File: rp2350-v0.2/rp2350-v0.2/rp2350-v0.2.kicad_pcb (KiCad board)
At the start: 4 copper layers, 65 x 65 mm, 112 parts, among them IC1 M95512-RMN6TP, IC2 TFBS4711-TT1, IC3 BQ25628ERYKR, IC4 RT6150B-33GQW, IC5 W25Q128JVSIM_TR, J1 USB_C_Receptacle_USB2.0_16P, J2 SWD, J3 BAT, J4 DO0180FMST08, J5 DBG_UART, J6 SPEAKER_CONNECTOR, SW1 BUT_R, SW2 BUT_M, SW3 BUT_L, SW4 SW_Push, U1 RP2350A-QFN60, Y1 ABM8-272-T3, Y2 SIT1533AI-H4-DCC-32.768E

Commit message: v0.2: loads of progress now gonna change it all up again
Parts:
- R34: value R -> 1k
- TP3: value GP28 -> GP26
- moved R23 15.4 mm to (166.2, 65.3), turned to 90 degrees
- moved JP1 12.2 mm to (179.8, 106.2)
- moved R20 9.06 mm to (159.2, 74.6), turned to 90 degrees
- moved R3 7.91 mm to (172.6, 95.0), turned to 0 degrees
- moved R5 7.69 mm to (143.8, 54.1), turned to 90 degrees
- moved C1 7.27 mm to (167.5, 104.6)
- moved C3 7.08 mm to (138.9, 53.8), turned to 180 degrees
- moved C2 6.95 mm to (145.4, 53.6)
- moved R4 6.76 mm to (162.9, 93.5), turned to 180 degrees
- moved JP3 6.73 mm to (170.7, 85.6), turned to 180 degrees
- moved C19 6.07 mm to (169.4, 73.9), turned to 90 degrees
- moved R13 5.83 mm to (97.6, 99.7)
- moved TH1 5.79 mm to (99.7, 104.0)
- moved TP1 5.76 mm to (128.7, 99.2)
- moved C5 5.69 mm to (164.9, 92.0), turned to 180 degrees
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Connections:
- R34 pad 1: Net-(U1-GPIO29_ADC3) -> /mcu/GPIO25
- TP3 pad 1: /mcu/GPIO28 -> /mcu/GPIO26
- U1 pad 12: /irda/IRDA.SD -> /mcu/QSPI1.SCK
- U1 pad 13: /irda/IRDA.RX -> /mcu/QSPI1.SDIO3
- U1 pad 14: /irda/IRDA.TX -> /mcu/QSPI1.SDIO2
- U1 pad 15: /buttons/BUT.L -> /mcu/QSPI1.SDIO1
- U1 pad 17: /mcu/QSPI1.SDIO1 -> /irda/IRDA.SD
- U1 pad 18: /mcu/QSPI1.SDIO2 -> /irda/IRDA.RX
- U1 pad 19: /mcu/QSPI1.SDIO3 -> /irda/IRDA.TX
- U1 pad 27: /mcu/QSPI1.SCK -> /buttons/BUT.L
- U1 pad 36: /mcu/PWR_AUX.~{BAT_CE} -> /mcu/SOUND_PWM
- U1 pad 37: /mcu/PWR_AUX.~{BAT_INT} -> /mcu/GPIO25
- U1 pad 40: /buttons/BUT.R -> /mcu/GPIO26
- U1 pad 41: /mcu/SOUND_PWM -> /buttons/BUT.R
- U1 pad 42: /mcu/GPIO28 -> /mcu/PWR_AUX.~{BAT_INT}
- U1 pad 43: Net-(U1-GPIO29_ADC3) -> /mcu/PWR_AUX.~{BAT_CE}
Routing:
- net /mcu/PWR_AUX.~{BAT_INT}: track 1.66 -> 50.4 mm, vias 1 -> 2
- net /accel/SPI.SCK: track 6.66 -> 48.3 mm
- net /mcu/I2C.SCL: track 3.07 -> 44.6 mm, vias 1 -> 2
- net /mcu/PWR_AUX.~{BAT_CE}: track 4.82 -> 44.4 mm, vias 1 -> 2
- net /mcu/I2C.SDA: track 3.27 -> 42.8 mm, vias 1 -> 2
- net /eeprom/~{EEPROM_CSB}: track 4.76 -> 43.7 mm, vias 0 -> 2
- net /connectors/DBG_UART.RX: track 0.00 -> 37.8 mm
- net /connectors/DBG_UART.TX: track 0.00 -> 37.0 mm
- net /accel/~{ACCEL_CSB}: track 0.00 -> 35.8 mm, vias 0 -> 2
- net /accel/SPI.MISO: track 5.83 -> 41.1 mm
- net /accel/ACCEL_INT: track 0.00 -> 33.7 mm, vias 0 -> 2
- net /mcu/SCREEN_AUX.~{RST}: track 1.51 -> 29.9 mm, vias 0 -> 2
- net /accel/SPI.MOSI: track 7.92 -> 36.2 mm, vias 0 -> 2
- net /mcu/SCREEN_AUX.~{CSB}: track 2.02 -> 28.0 mm, vias 0 -> 2
- net /mcu/QSPI1.SCK: track 1.53 -> 26.0 mm
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- added copper zone on In2.Cu, net /accel/ACCEL_3V3
- added copper zone on In2.Cu, net /irda/IRDA_3V3
- added copper zone on F.Cu, net /screen/SCREEN_VSYS

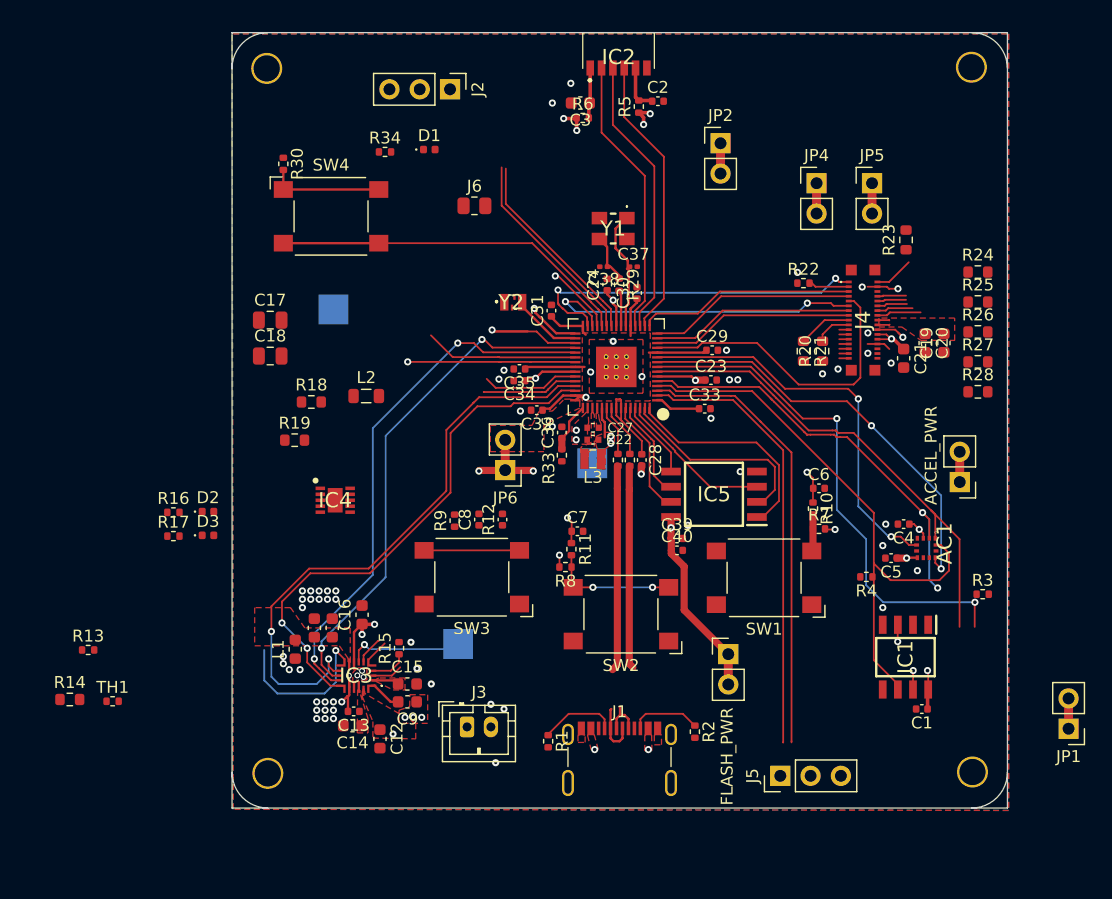
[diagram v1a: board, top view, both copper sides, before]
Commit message: v0.2: more progress on routing, nearly done
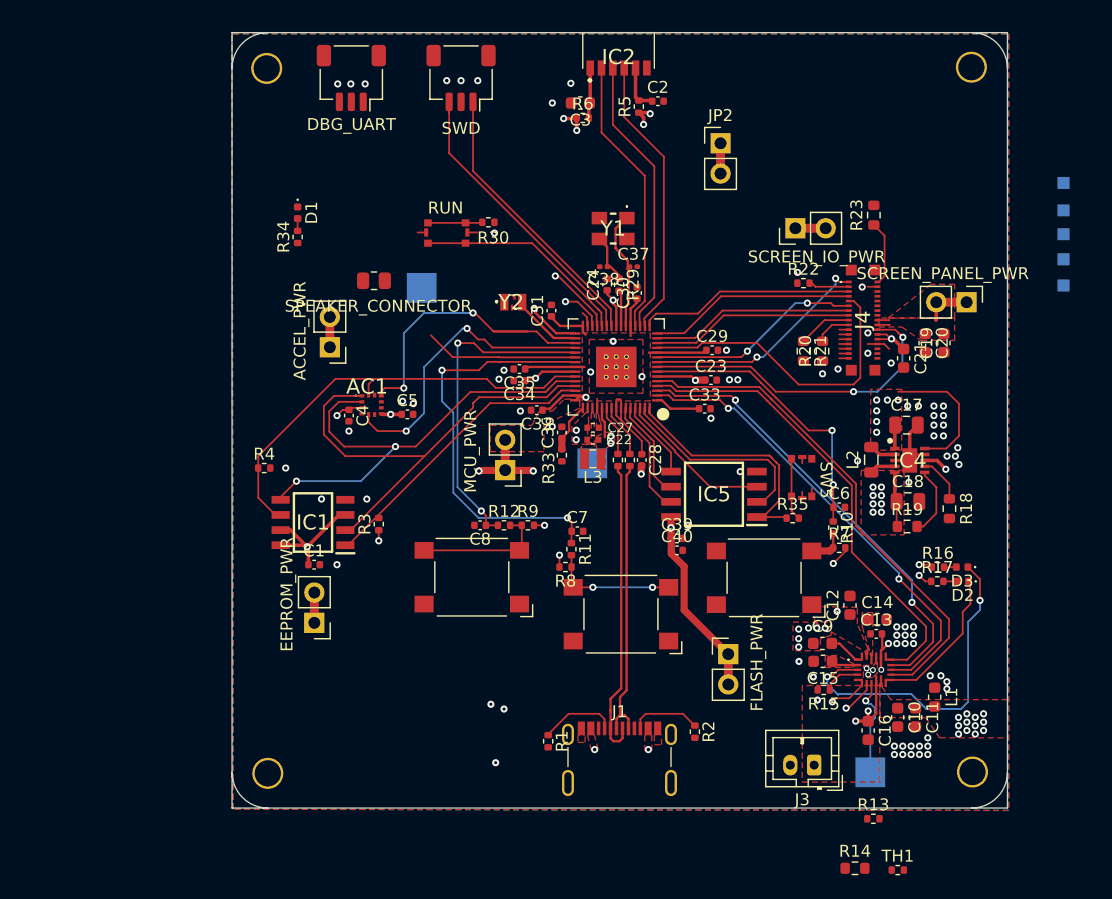
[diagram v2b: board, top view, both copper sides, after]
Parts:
- removed R24, R25, R26, R27, R28: 0R, Resistor_SMD:R_0603_1608Metric
- added R35: 1k, Resistor_SMD:R_0402_1005Metric, F.Cu at (156.7, 88.6)
- added SW5: BOOTSEL, CustomFootprints:WS_TASV_435151014824, F.Cu at (158.3, 85.2)
- added TP4: TP_SDA, TestPoint:TestPoint_Pad_1.0x1.0mm, B.Cu at (179.4, 62.8)
- added TP5: TP_SCL, TestPoint:TestPoint_Pad_1.0x1.0mm, B.Cu at (179.4, 60.5)
- added TP6: TP_INT, TestPoint:TestPoint_Pad_1.0x1.0mm, B.Cu at (179.4, 64.8)
- added TP7: TP_RESET, TestPoint:TestPoint_Pad_1.0x1.0mm, B.Cu at (179.4, 66.9)
- added TP8: TP_VCC, TestPoint:TestPoint_Pad_1.0x1.0mm, B.Cu at (179.4, 69.1)
- J2, J5: footprint Connector_PinHeader_2.54mm:PinHeader_1x03_P2.54mm_Vertical -> Connector_JST:JST_SH_SM03B-SRSS-TB_1x03-1MP_P1.00mm_Horizontal
- R12: footprint Capacitor_SMD:C_0402_1005Metric -> Resistor_SMD:R_0402_1005Metric
- R31, R32: value R -> 22R
- SW4: value SW_Push -> RUN; footprint Button_Switch_SMD:SW_SPST_Omron_B3FS-101xP -> CustomFootprints:WS_TASV_435151014824
- moved J5 68.7 mm to (119.7, 51.7), turned to 180 degrees
- moved R13 67.3 mm to (163.5, 113.8)
- moved R14 67.3 mm to (161.9, 118.0)
- moved TH1 67.3 mm to (165.5, 118.1)
- moved R16 64.2 mm to (168.9, 92.7)
- moved R17 64.1 mm to (168.8, 93.9)
- moved JP1 63.8 mm to (116.6, 97.4)
- moved D2 63.5 mm to (171.0, 93.9), turned to 180 degrees
- moved D3 63.3 mm to (170.9, 92.7), turned to 180 degrees
- moved C18 54.8 mm to (166.4, 87.2)
- moved R18 54.2 mm to (169.8, 87.8), turned to -90 degrees
- moved C17 54.1 mm to (166.2, 80.8)
- moved JP3 54.0 mm to (117.9, 74.3)
- moved L1 53.7 mm to (168.6, 103.6), turned to -90 degrees
- moved C1 52.4 mm to (116.6, 92.5), turned to 0 degrees
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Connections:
- net /connectors/USB.DM renamed /connectors/USB.D-
- net /connectors/USB.DP renamed /connectors/USB.D+
- J4 pad 10: Net-(J4-TP_SDA) -> /screen/TP_I2C.SDA
- J4 pad 12: Net-(J4-TP_INT) -> /screen/TP_AUX.INT
- J4 pad 14: Net-(J4-TP_RESET) -> /screen/TP_AUX.RESET
- J4 pad 16: Net-(J4-TP_VCC) -> /screen/SCREEN_3V3
- J4 pad 8: Net-(J4-TP_SCL) -> /screen/TP_I2C.SCL
- J5 pad 1: /connectors/DBG_UART.TX -> /connectors/DBG_UART.RX
- J5 pad 3: /connectors/DBG_UART.RX -> /connectors/DBG_UART.TX
- SW4 pad 2: Net-(U1-RUN) -> Net-(R30-Pad2)
- U1 pad 10: /accel/ACCEL_INT -> /mcu/SCREEN_AUX.~{CSB}
- U1 pad 2: /connectors/DBG_UART.TX -> /mcu/I2C.SDA
- U1 pad 27: /buttons/BUT.L -> /connectors/DBG_UART.TX
- U1 pad 28: /mcu/SCREEN_AUX.~{CSB} -> /connectors/DBG_UART.RX
- U1 pad 29: /mcu/SCREEN_AUX.~{RST} -> unconnected-(U1-GPIO18-Pad29)
- U1 pad 3: /connectors/DBG_UART.RX -> /mcu/I2C.SCL
- U1 pad 31: /mcu/SCREEN_AUX.PWR_EN -> unconnected-(U1-GPIO19-Pad31)
- U1 pad 33: /buttons/BUT.M -> /accel/~{ACCEL_CSB}
- U1 pad 34: /mcu/I2C.SDA -> /accel/ACCEL_INT
- U1 pad 35: /mcu/I2C.SCL -> /buttons/BUT.L
- U1 pad 37: /mcu/GPIO25 -> /buttons/BUT.M
- U1 pad 4: /accel/SPI.SCK -> /mcu/PWR_AUX.~{BAT_CE}
- U1 pad 40: /mcu/GPIO26 -> /accel/SPI.SCK
- U1 pad 41: /buttons/BUT.R -> /accel/SPI.MOSI
- U1 pad 42: /mcu/PWR_AUX.~{BAT_INT} -> /accel/SPI.MISO
- U1 pad 43: /mcu/PWR_AUX.~{BAT_CE} -> /eeprom/~{EEPROM_CSB}
- U1 pad 5: /accel/SPI.MOSI -> /mcu/PWR_AUX.~{BAT_INT}
- U1 pad 7: /accel/SPI.MISO -> /buttons/BUT.R
- U1 pad 8: /eeprom/~{EEPROM_CSB} -> /mcu/SCREEN_AUX.PWR_EN
- U1 pad 9: /accel/~{ACCEL_CSB} -> /mcu/SCREEN_AUX.~{RST}
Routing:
- net /connectors/DBG_UART.RX: track 37.8 -> 3.51 mm, vias 0 -> 1
- net /connectors/DBG_UART.TX: track 37.0 -> 5.74 mm, vias 0 -> 1
- net /power/~{PG}: track 2.60 -> 28.3 mm, vias 0 -> 2
- net /buttons/BUT.M: track 12.5 -> 35.0 mm
- net /buttons/BUT.L: track 5.74 -> 27.4 mm, vias 1 -> 2
- net /mcu/SCREEN_AUX.PWR_EN: track 7.38 -> 27.8 mm
- net /eeprom/~{EEPROM_CSB}: track 43.7 -> 24.6 mm, vias 2 -> 0
- net +3.3V: track 6.46 -> 24.1 mm, vias 4 -> 13
- net /mcu/GPIO25: track 14.2 -> 0.00 mm, vias 1 -> 0
- net /buttons/BUT.R: track 10.8 -> 24.5 mm, vias 1 -> 2
- net Net-(U1-RUN): track 30.2 -> 18.1 mm
- net /accel/SPI.SCK: track 48.3 -> 37.6 mm
- net /mcu/SCREEN_AUX.~{RST}: track 29.9 -> 19.4 mm
- net /mcu/SCREEN_AUX.~{CSB}: track 28.0 -> 18.1 mm
- net /accel/~{ACCEL_CSB}: track 35.8 -> 25.9 mm
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- added copper zone on F.Cu, net +3.3V
- added copper zone on F.Cu, net /connectors/BAT+
- added copper zone on In2.Cu, net /screen/SCREEN_3V3
- added copper zone on In2.Cu, net VSYS
- removed copper zone on In2.Cu, net /connectors/BAT+
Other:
- board text removed: "500 mAh battery"

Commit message: v0.2: routing done, nearly ready for prod
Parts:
- added TP9: GP18, TestPoint:TestPoint_Pad_2.5x2.5mm, B.Cu at (119.8, 66.5)
- D1: value LED -> USER_LED
- JP4: value SCREEN_IO_PWR -> IO_PWR
- JP5: value SCREEN_PANEL_PWR -> PANEL_PWR
- TP3: value GP26 -> GP19
- moved TH1 44.9 mm to (122.8, 104.1), turned to 180 degrees
- moved R13 40.6 mm to (124.5, 102.4), turned to -90 degrees
- moved R14 39.2 mm to (124.5, 106.4), turned to -90 degrees
- moved J6 8.34 mm to (113.3, 67.9), turned to 90 degrees
- moved TP4 7.63 mm to (172.3, 60.0)
- moved TP8 7.63 mm to (172.3, 66.3)
- moved TP7 7.60 mm to (172.3, 64.2)
- moved TP6 7.60 mm to (172.3, 62.1)
- moved TP5 7.56 mm to (172.3, 57.9)
- moved C2 0.60 mm to (145.4, 54.2)
- moved C3 0.60 mm to (138.9, 54.4)
- moved IC2 0.60 mm to (142.1, 50.0)
- moved R5 0.60 mm to (143.8, 54.7)
- moved R6 0.60 mm to (139.1, 55.6)
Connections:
- R34 pad 1: /mcu/GPIO25 -> /mcu/GPIO18
- TP3 pad 1: /mcu/GPIO26 -> /mcu/GPIO19
- U1 pad 29: unconnected-(U1-GPIO18-Pad29) -> /mcu/GPIO18
- U1 pad 31: unconnected-(U1-GPIO19-Pad31) -> /mcu/GPIO19
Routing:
- net /power/TS: track 2.90 -> 44.2 mm, vias 1 -> 2
- net /power/TS_BIAS: track 3.04 -> 39.8 mm, vias 1 -> 2
- net /mcu/GPIO18: track 0.00 -> 33.0 mm, vias 0 -> 1
- net /connectors/DBG_UART.TX: track 5.74 -> 33.2 mm, vias 1 -> 2
- net /connectors/DBG_UART.RX: track 3.51 -> 30.8 mm, vias 1 -> 2
- net /screen/TP_I2C.SCL: track 0.00 -> 16.9 mm, vias 0 -> 1
- net /screen/TP_I2C.SDA: track 0.00 -> 15.5 mm, vias 0 -> 1
- net /mcu/SOUND_PWM: track 12.9 -> 27.8 mm
- net /mcu/GPIO19: track 0.00 -> 14.6 mm, vias 0 -> 1
- net /screen/SCREEN_3V3: track 3.84 -> 18.4 mm, vias 1 -> 3
- net /screen/TP_AUX.INT: track 0.00 -> 13.5 mm, vias 0 -> 1
- net /screen/TP_AUX.RESET: track 0.00 -> 12.3 mm, vias 0 -> 1
- net /mcu/MCU_3V3: track 34.3 -> 38.7 mm, vias 1 -> 0
- net unconnected-(U1-GPIO19-Pad31): track 4.41 -> 0.00 mm, vias 1 -> 0
- net /mcu/MCU_1V1: track 27.5 -> 31.6 mm, vias 8 -> 9
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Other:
- outline, holes or cut-outs redrawn
- board text added: "picowalker v0.2"
- board text added: "picowalker v0.2 by mamba2410"

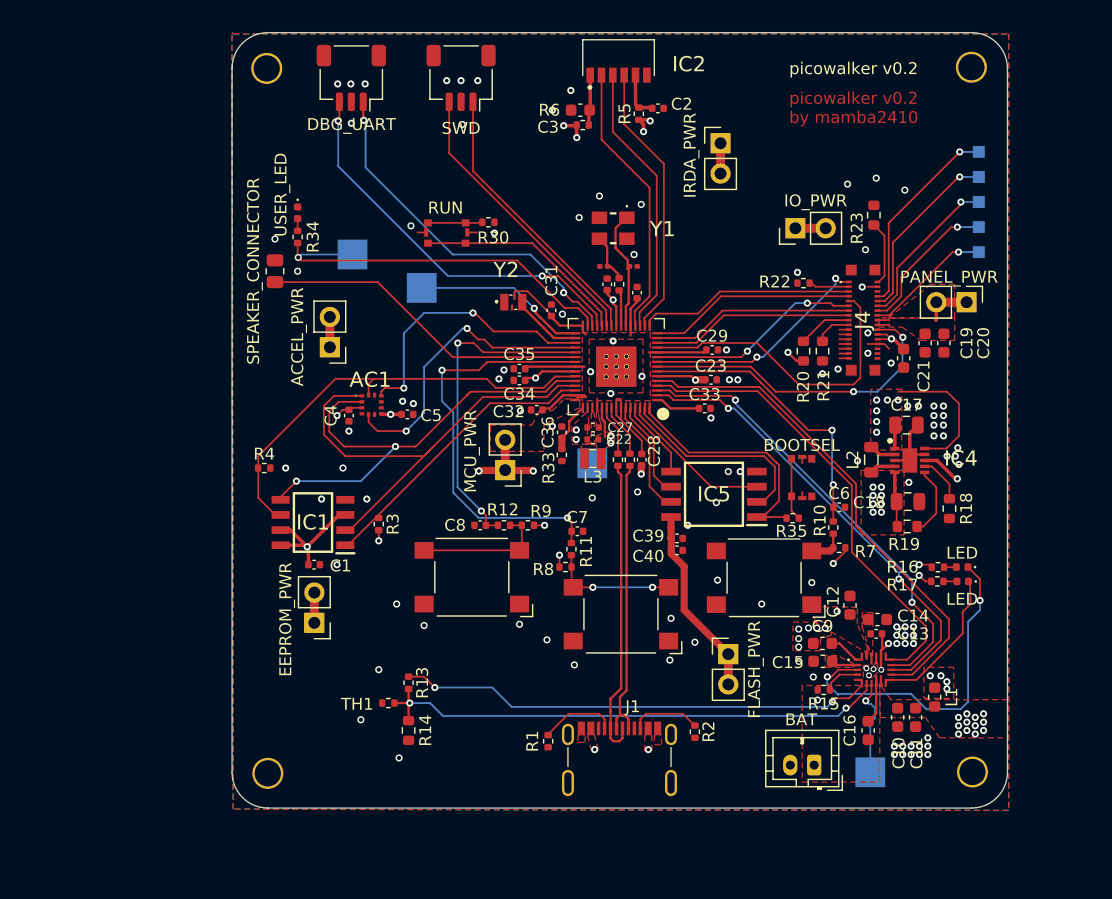
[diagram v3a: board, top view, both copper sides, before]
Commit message: v0.2: final big checks done, fixed IrDA footprint
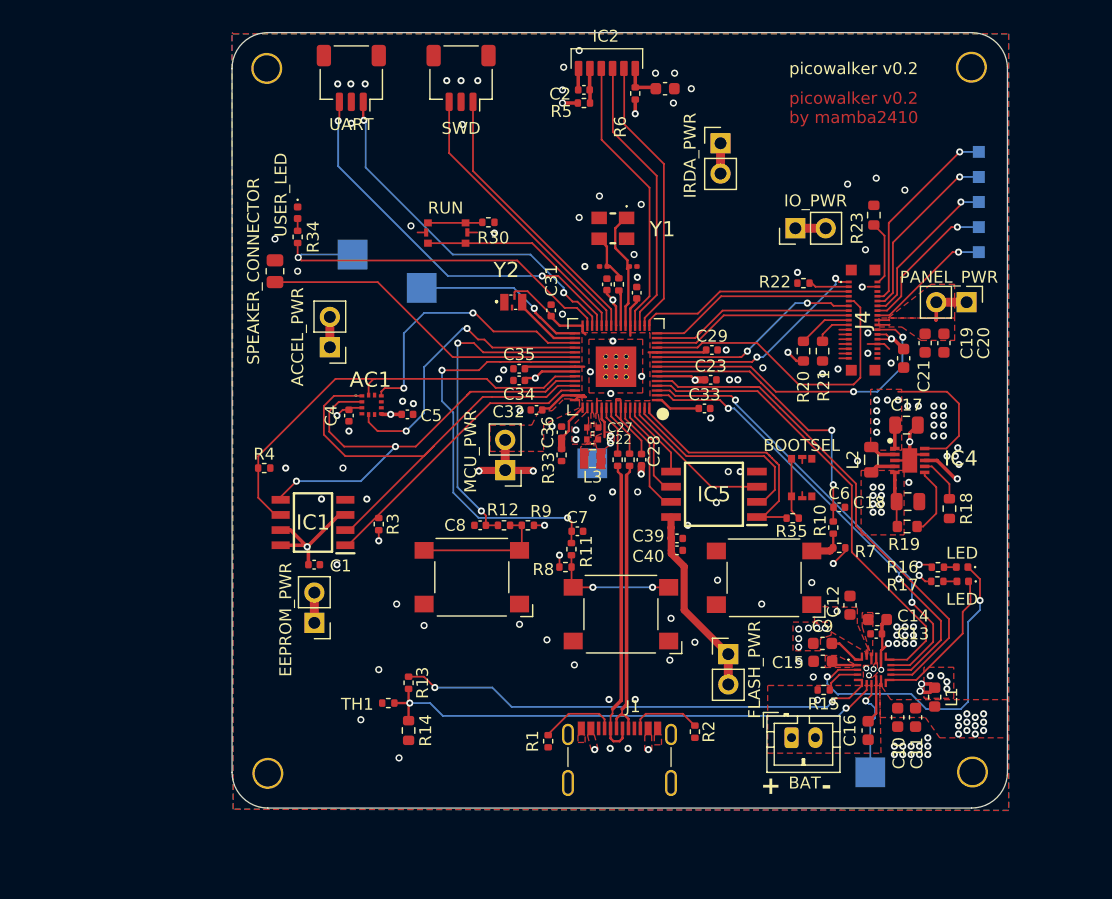
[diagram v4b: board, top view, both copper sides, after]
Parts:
- IC2: footprint SamacSys_Parts:TFBS4711TT1 -> CustomFootprints:TFBS4711-TR
- J1: value USB_C_Receptacle_USB2.0_16P -> USB4215-03-A
- J5: value DBG_UART -> UART
- L2: value L -> 2.2uH
- moved C3 7.32 mm to (146.0, 52.6), turned to 0 degrees
- moved C2 6.39 mm to (139.2, 52.7), turned to 180 degrees
- moved R6 5.14 mm to (143.5, 53.0), turned to 90 degrees
- moved R5 4.69 mm to (139.2, 53.8), turned to 0 degrees
- moved J3 2.98 mm to (156.6, 107.0), turned to 0 degrees
- moved IC2 1.33 mm to (141.1, 50.9)
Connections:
- U1 pad 17: /irda/IRDA.SD -> /irda/IRDA.TX
- U1 pad 19: /irda/IRDA.TX -> /irda/IRDA.SD
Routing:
- net GND: track 21.5 -> 24.6 mm, vias 110 -> 124
- net /power/SW: track 0.00 -> 2.49 mm, vias 13 -> 15
- net /irda/IRDA_3V3: track 4.31 -> 2.48 mm, vias 4 -> 2
- net Net-(IC2-VCC1): track 3.98 -> 2.92 mm
- net Net-(IC2-VCC2/IRED/ANODE): track 4.23 -> 3.36 mm
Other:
- board text added: "+"
- board text added: "-"

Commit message: v0.2: update battery connector and labels
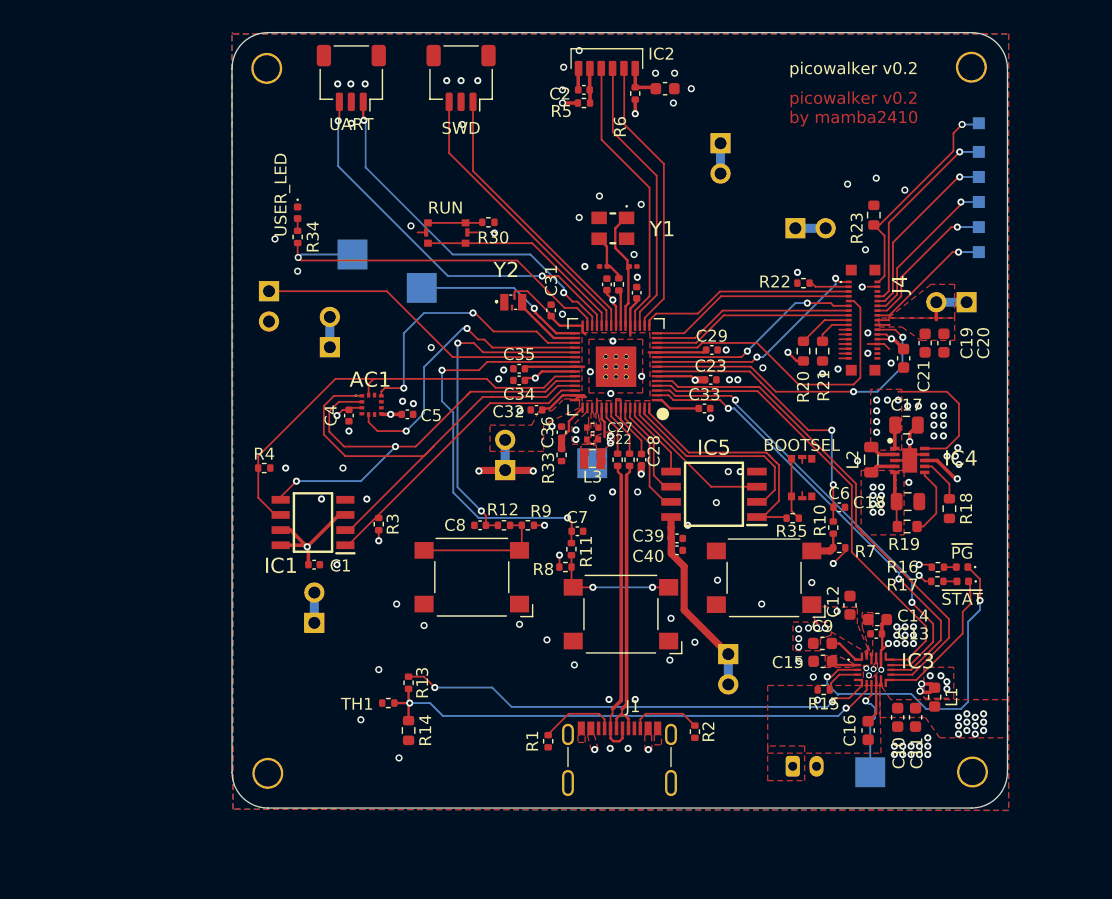
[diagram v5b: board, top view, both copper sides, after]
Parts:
- added TP10: TE, TestPoint:TestPoint_Pad_1.0x1.0mm, B.Cu at (172.3, 55.5)
- D2: value LED -> ~{STAT}
- D3: value LED -> ~{PG}
- J3: footprint Connector_JST:JST_PH_B2B-PH-K_1x02_P2.00mm_Vertical -> Connector_JST:JST_PH_S2B-PH-K_1x02_P2.00mm_Horizontal; moved to B.Cu
- J6: footprint Resistor_SMD:R_0805_2012Metric -> Connector_PinHeader_2.54mm:PinHeader_1x02_P2.54mm_Vertical; moved to B.Cu
- JP1, JP2, JP3, JP4, JP5, JP6, JP7: moved to B.Cu
- moved J3 2.40 mm to (156.7, 109.4)
- moved J6 1.75 mm to (112.8, 69.6), turned to 180 degrees
- turned JP1 to 0 degrees
- turned JP2 to 180 degrees
- turned JP3 to 0 degrees
- turned JP4 to -90 degrees
- turned JP5 to 90 degrees
- turned JP6 to 0 degrees
- turned JP7 to 180 degrees
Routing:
- net Net-(J4-TE): track 5.45 -> 18.7 mm, vias 0 -> 1
- net GND: vias 124 -> 125
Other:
- board text added: "Battery 503035"

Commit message: v0.2: minor position adjustments
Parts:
- moved C2 1.08 mm to (140.3, 52.7)
- moved R5 1.08 mm to (140.3, 53.8)
- moved C3 1.07 mm to (147.1, 52.6)
- moved IC2 1.07 mm to (142.2, 50.9)
- moved R6 1.07 mm to (144.6, 53.0)
- moved SW2 0.21 mm to (142.1, 96.7)
- moved SW3 0.10 mm to (129.9, 93.5)
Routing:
- net GND: track 24.6 -> 25.2 mm, vias 125 -> 196

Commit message: v0.2: sent to jlc
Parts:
- added R24: 10k, Resistor_SMD:R_0402_1005Metric, F.Cu at (151.2, 81.0)
- added R25: 10k, Resistor_SMD:R_0402_1005Metric, F.Cu at (153.2, 81.0)
- R22: footprint Resistor_SMD:R_0402_1005Metric -> Resistor_SMD:R_0603_1608Metric
- R29: value R -> 1k
- moved TH1 5.60 mm to (122.8, 98.5), turned to 90 degrees
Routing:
- net /power/TS: track 44.2 -> 48.8 mm
- net /mcu/I2C.SCL: track 38.4 -> 40.8 mm
- net +3.3V: track 24.1 -> 26.2 mm, vias 13 -> 15
- net /mcu/I2C.SDA: track 38.8 -> 39.9 mm
- net GND: vias 196 -> 213
